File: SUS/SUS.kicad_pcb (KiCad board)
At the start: 4 copper layers, 117.7 x 30.4 mm, 72 parts, among them J1 ESP32_Connector_0, J2 ESP32_Connector_1, J3 I2C, J4 I2C, J5 I2C, J6 ADC, J7 WS, U1 TJA1051T, U2 ADS8320EB_250, U3 ICM-42688-P, U4 S1001-46R, U5 S1001-46R, U6 S1001-46R

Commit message: Complete re-design. Readme still needs to be updated.
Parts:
- removed the G*** at (106.8, 58.1)
- removed the G*** at (106.6, 59.9)
- removed the G*** at (148.9, 60.0)
- removed the G*** at (96.6, 60.1)
- removed H4: MountingHole, MountingHole:MountingHole_2.7mm_M2.5
- removed J4, J5: I2C, Connector_Hirose:Hirose_DF3EA-04P-2H_1x04-1MP_P2.00mm_Horizontal
- removed J6: ADC, Connector_Hirose:Hirose_DF3EA-03P-2H_1x03-1MP_P2.00mm_Horizontal
- removed J7: WS, Connector_Hirose:Hirose_DF3EA-03P-2H_1x03-1MP_P2.00mm_Horizontal
- removed R27: 0, Resistor_SMD:R_0402_1005Metric_Pad0.72x0.64mm_HandSolder
- removed U5, U6: S1001-46R, S1001-46R:S100146R
- added C26: 10μF, Capacitor_SMD:C_0603_1608Metric, F.Cu at (126.0, 52.5)
- added C27: 10μF, Capacitor_SMD:C_0603_1608Metric, F.Cu at (131.0, 55.2)
- added C28: 0.1μF, Capacitor_SMD:C_0201_0603Metric, F.Cu at (99.6, 54.1)
- added G***: LOGO, LOGO, F.Cu at (116.4, 55.8)
- added G***: LOGO, LOGO, F.Cu at (86.5, 56.0)
- added G***: LOGO, LOGO, F.Cu at (116.6, 54.0)
- added JP1: SolderJumper_2_Open, Jumper:SolderJumper-2_P1.3mm_Open_TrianglePad1.0x1.5mm, B.Cu at (128.1, 78.3)
- added R25: 10k, Capacitor_SMD:C_0201_0603Metric, F.Cu at (106.1, 67.7)
- C1: value 10μF -> 0.1μF; footprint Capacitor_SMD:C_0402_1005Metric_Pad0.74x0.62mm_HandSolder -> Capacitor_SMD:C_0201_0603Metric
- C2: value 1μF -> 0.1μF; footprint Capacitor_SMD:C_0402_1005Metric_Pad0.74x0.62mm_HandSolder -> Capacitor_SMD:C_0201_0603Metric
- C3: value 2.2μF -> 10nF; footprint Capacitor_SMD:C_0402_1005Metric_Pad0.74x0.62mm_HandSolder -> Capacitor_SMD:C_0201_0603Metric
- C4: value 0.1μF -> 2.2μF; footprint Capacitor_SMD:C_0402_1005Metric_Pad0.74x0.62mm_HandSolder -> Capacitor_SMD:C_0201_0603Metric
- C5: footprint Capacitor_SMD:C_0402_1005Metric_Pad0.74x0.62mm_HandSolder -> Capacitor_SMD:C_0201_0603Metric
- H1, H2, H3: value MountingHole -> MountingHole_Pad; footprint MountingHole:MountingHole_2.7mm_M2.5 -> MountingHole:MountingHole_2.2mm_M2_Pad_TopOnly
- J3: value I2C -> D25P13A4GV00LF; footprint Connector_Hirose:Hirose_DF3EA-04P-2H_1x04-1MP_P2.00mm_Horizontal -> D25:CONN_D25P_AMP
- R1, R2: footprint Resistor_SMD:R_0402_1005Metric_Pad0.72x0.64mm_HandSolder -> Capacitor_SMD:C_0201_0603Metric
- R23, R24: value 0 -> 10k; footprint Resistor_SMD:R_0402_1005Metric_Pad0.72x0.64mm_HandSolder -> Capacitor_SMD:C_0201_0603Metric
- U1: value TJA1051T -> HT7333; footprint Package_SO:SOIC-8_3.9x4.9mm_P1.27mm -> HT7333:IC_HT7333
- U2: value ADS8320EB_250 -> ADS1015IDGSR; footprint ADS8320EB_250:DGK0008A_L -> ADC:SOP50P490X110-10N
- U3: footprint IMU:ICM-42688-P -> IMU:PQFN50P300X250X97-14N
- U4: value S1001-46R -> TJA1051TK-3; footprint S1001-46R:S100146R -> Package_DFN_QFN:DFN-8-1EP_3x3mm_P0.65mm_EP1.55x2.4mm
- moved H3 101.3 mm to (132.0, 94.0)
- moved R3 65.8 mm to (134.1, 68.5), turned to 0 degrees
- moved R16 64.9 mm to (134.1, 70.5)
- moved C19 64.2 mm to (134.1, 71.4), turned to 0 degrees
- moved C6 63.7 mm to (133.0, 68.8)
- moved C18 63.6 mm to (133.0, 70.2)
- moved R17 63.5 mm to (134.1, 72.4), turned to 0 degrees
- moved R4 61.9 mm to (131.9, 68.5), turned to 0 degrees
- moved R15 61.5 mm to (131.9, 70.5), turned to 180 degrees
- moved C20 61.4 mm to (133.0, 72.1), turned to -90 degrees
- moved R1 59.9 mm to (118.2, 61.7), turned to 180 degrees
- moved C7 59.8 mm to (130.8, 68.8)
- moved R18 59.8 mm to (131.9, 72.4), turned to 0 degrees
- moved C17 59.7 mm to (130.8, 70.2)
- moved R5 58.0 mm to (129.7, 68.5), turned to 0 degrees
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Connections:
- C1 pad 1: +5V -> 5V
- C2 pad 1: +3.3V -> +5V
- J1 pad 16: CAN_S -> IMU_CS
- J1 pad 17: CAN_TX -> IMU_SCL
- J1 pad 18: CAN_RX -> IMU_MOSI
- J1 pad 19: unconnected-(J1-Pin_19-Pad19) -> IMU_MISO
- J1 pad 20: unconnected-(J1-Pin_20-Pad20) -> ESP_ADC
- J1 pad 4: I2C_SDA -> unconnected-(J1-Pin_4-Pad4)
- J1 pad 5: I2C_SCL -> unconnected-(J1-Pin_5-Pad5)
- J1 pad 7: /WS_IN -> unconnected-(J1-Pin_7-Pad7)
- J2 pad 10: IMU_MISO -> GPIO 38
- J2 pad 11: IMU_MOSI -> GPIO 37
- J2 pad 12: IMU_SCK -> GPIO 36
- J2 pad 13: IMU_CS -> GPIO 35
- J2 pad 16: unconnected-(J2-Pin_16-Pad16) -> I2C_SCL
- J2 pad 17: unconnected-(J2-Pin_17-Pad17) -> I2C_SDA
- J2 pad 19: unconnected-(J2-Pin_19-Pad19) -> GPIO 20
- J2 pad 2: unconnected-(J2-Pin_2-Pad2) -> TX
- J2 pad 20: unconnected-(J2-Pin_20-Pad20) -> GPIO 19
- J2 pad 3: unconnected-(J2-Pin_3-Pad3) -> RX
- J2 pad 4: Net-(J2-Pin_4) -> CAN_TX
- J2 pad 5: A_SCK -> CAN_RX
- J2 pad 6: A_MISO -> CAN_S
- J2 pad 7: A_CS -> A_SCL
- J2 pad 8: unconnected-(J2-Pin_8-Pad8) -> A_SDA
- J2 pad 9: unconnected-(J2-Pin_9-Pad9) -> A_CS
- J3 pad 1: +5V -> +12V
- J3 pad 2: GND -> GPIO 19
- J3 pad 3: CAN- -> GPIO 20
- J3 pad 4: CAN+ -> GND
- R23 pad 2: Net-(J6-Pin_1) -> A_SCL
- R24 pad 1: +5V -> +3.3V
- R24 pad 2: Net-(J6-Pin_1) -> A_SDA
- U1 pad 1: CAN_TX -> GND
- U1 pad 2: GND -> +12V
- U2 pad 1: +5V -> GND
- U2 pad 2: AA_out -> A_CS
- U2 pad 4: GND -> AA_out
- U2 pad 5: A_CS -> GND
- U2 pad 6: A_MISO -> unconnected-(U2-AIN2-Pad6)
- U2 pad 7: A_SCK -> unconnected-(U2-AIN3-Pad7)
- U2 pad 8: +3.3V -> 5V
- U3 pad 13: IMU_SCK -> IMU_SCL
- U4 pad 1: GND -> CAN_TX
- U4 pad 3: GND -> +5V
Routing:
- net GND: track 99.6 -> 47.6 mm, vias 71 -> 14
- net /WS_IN: track 44.5 -> 0.00 mm
- net CAN+: track 53.4 -> 10.9 mm
- net CAN-: track 52.6 -> 11.0 mm
- net GPIO 20: track 0.00 -> 20.6 mm
- net GPIO 19: track 0.00 -> 20.5 mm
- net RX: track 0.00 -> 20.5 mm
- net TX: track 0.00 -> 20.4 mm
- net GPIO 36: track 0.00 -> 19.1 mm
- net GPIO 37: track 0.00 -> 18.5 mm
- net A_In: track 18.1 -> 36.5 mm
- net A_SCL: track 0.00 -> 18.2 mm
- net GPIO 35: track 0.00 -> 18.0 mm
- net GPIO 38: track 0.00 -> 17.7 mm
- net A_SDA: track 0.00 -> 14.1 mm
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- added copper zone on B.Cu, net +3.3V
- added copper zone on In1.Cu, net +5V
- removed copper zone on In1.Cu, net +3.3V
- removed copper zone on B.Cu, net +5V
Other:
- board size 117.7 x 30.4 mm -> 58 x 64 mm
- board text added: "12V"
- board text added: "19"
- board text added: "20"
- board text added: "35"
- board text added: "36"
- board text added: "37"
- board text added: "38"
- board text added: "A_IN"
- board text added: "CH"
- board text added: "CL"
- board text added: "NC"
- board text added: "RX"
- board text added: "SCL"
- board text added: "SDA"
- board text added: "TX"
- board text removed: "CAN"
- board text removed: "DLHR"
- board text removed: "ESP_ADC"
- board text removed: "LP"
- board text removed: "U3"
- board text removed: "WS"

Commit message: Updated Readme
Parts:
- moved H1 0.89 mm to (107.0, 55.0)
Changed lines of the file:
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@@
 	(footprint "MountingHole:MountingHole_2.2mm_M2_Pad_TopOnly"
 		(layer "F.Cu")
-		(at 107.4 55.8)
+		(at 107 55)
 		(descr "Mounting Hole 2.2mm, M2")
 		(tags "mounting hole 2.2mm m2")
@@
 		(layer "Edge.Cuts")
 	)
+	(gr_line
+		(start 107 94)
+		(end 107 96)
+		(stroke
+			(width 0.1)
+			(type default)
+		)
+		(layer "User.1")
+	)
+	(gr_line
+		(start 107 55)
+		(end 107 94)
+		(stroke
+			(width 0.1)
+			(type default)
+		)
+		(layer "User.1")
+	)
 	(gr_text "CH"
 		(at 96.2 48.9 0)
@@
 		)
 	)
+	(dimension
+		(type aligned)
+		(layer "User.1")
+		(pts
+			(xy 132 94) (xy 82 94)
+		)
+		(height -7)
+		(gr_text "50.0000 mm"
+			(at 107 99.85 0)
+			(layer "User.1")
+			(effects
+				(font
+					(size 1 1)
+					(thickness 0.15)
+				)
+			)
+		)
+		(format
+			(prefix "")
+			(suffix "")
+			(units 3)
+			(units_format 1)
+			(precision 4)
+		)
+		(style
+			(thickness 0.1)
+			(arrow_length 1.27)
+			(text_position_mode 0)
+			(extension_height 0.58642)
+			(extension_offset 0.5) keep_text_aligned)
+	)
+	(dimension
+		(type aligned)
+		(layer "User.1")
+		(pts
+			(xy 107 55) (xy 107 94)
+		)
+		(height 38)
+		(gr_text "39.0000 mm"
+			(at 67.85 74.5 90)
+			(layer "User.1")
+			(effects
+				(font
+					(size 1 1)
+					(thickness 0.15)
+				)
+			)
+		)
+		(format
+			(prefix "")
+			(suffix "")
+			(units 3)
+			(units_format 1)
+			(precision 4)
+		)
+		(style
+			(thickness 0.1)
+			(arrow_length 1.27)
+			(text_position_mode 0)
+			(extension_height 0.58642)
+			(extension_offset 0.5) keep_text_aligned)
+	)
+	(dimension
+		(type aligned)
+		(layer "User.1")
+		(pts
+			(xy 107 94) (xy 82 94)
+		)
+		(height -4)
+		(gr_text "25.0000 mm"
+			(at 94.5 96.85 0)
+			(layer "User.1")
+			(effects
+				(font
+					(size 1 1)
+					(thickness 0.15)
+				)
+			)
+		)
+		(format
+			(prefix "")
+			(suffix "")
+			(units 3)
+			(units_format 1)
+			(precision 4)
+		)
+		(style
+			(thickness 0.1)
+			(arrow_length 1.27)
+			(text_position_mode 0)
+			(extension_height 0.58642)
+			(extension_offset 0.5) keep_text_aligned)
+	)
 	(segment
 		(start 110 81.226898)
@@
 	)
 	(segment
-		(start 104.35 48.974144)
-		(end 104.35 63.25)
+		(start 104 62.9)
+		(end 105.2 64.1)
 		(width 0.3)
 		(layer "F.Cu")
@@
 	)
 	(segment
-		(start 104.35 63.25)
-		(end 105.2 64.1)
+		(start 106.479994 46.84415)
+		(end 104 49.324144)
 		(width 0.3)
 		(layer "F.Cu")
@@
 	)
 	(segment
-		(start 106.479994 46.84415)
-		(end 104.35 48.974144)
+		(start 104 49.324144)
+		(end 104 62.9)
 		(width 0.3)
 		(layer "F.Cu")

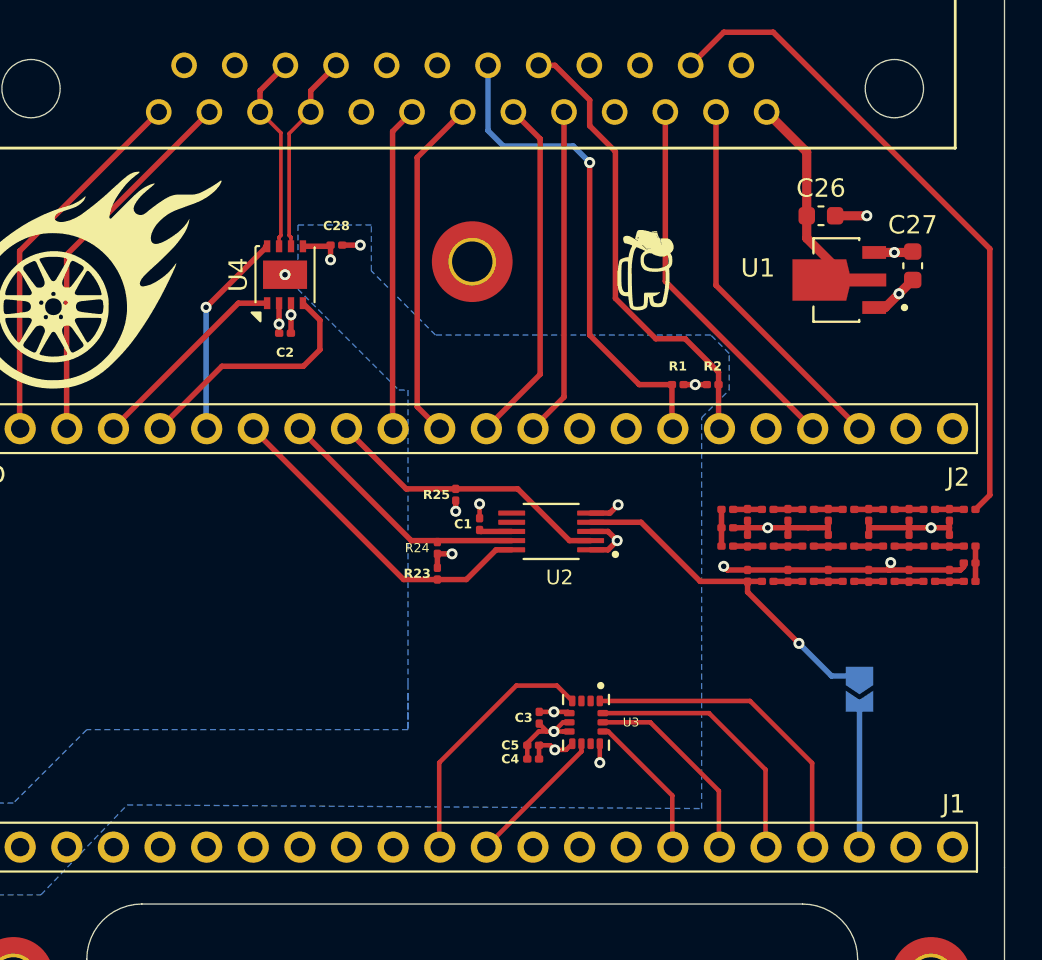
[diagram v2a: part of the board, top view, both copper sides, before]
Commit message: Changed CAN transceiver.
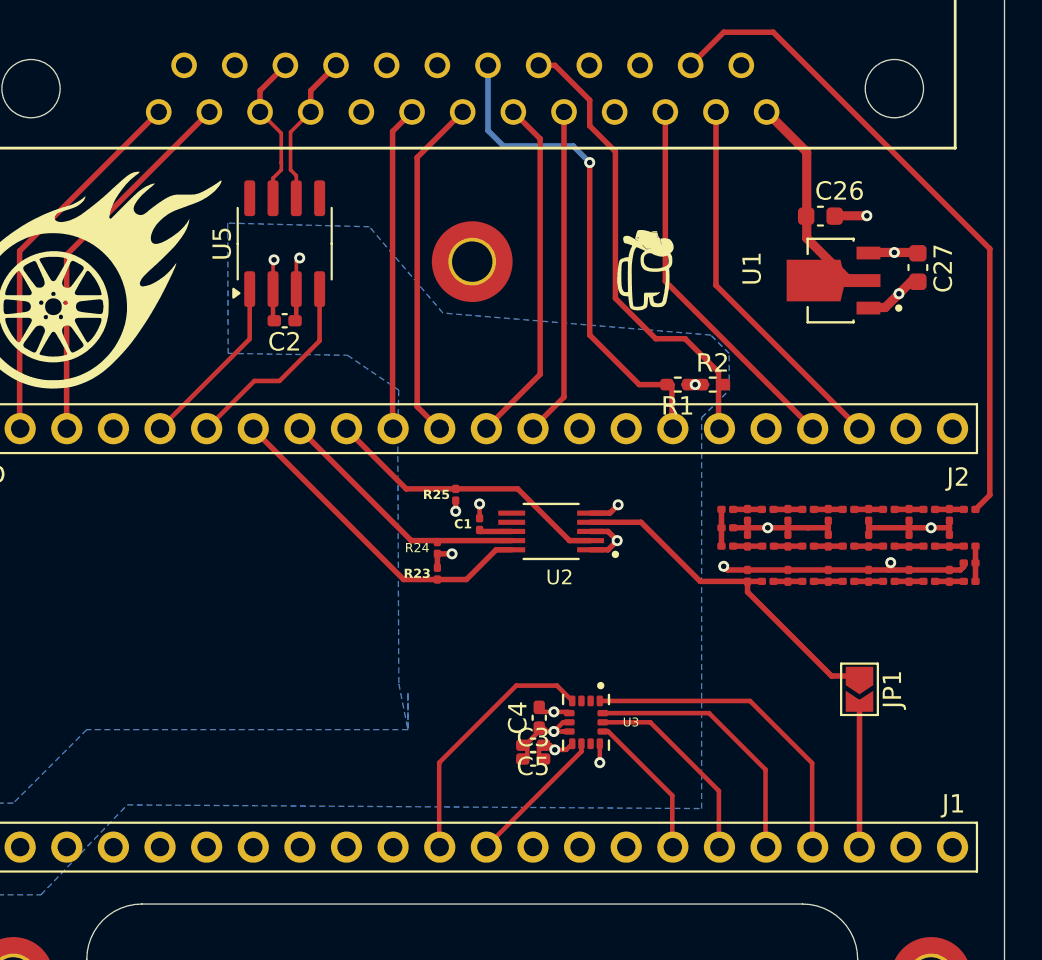
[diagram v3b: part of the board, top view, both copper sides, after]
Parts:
- removed C28: 0.1μF, Capacitor_SMD:C_0201_0603Metric
- removed U4: TJA1051TK-3, Package_DFN_QFN:DFN-8-1EP_3x3mm_P0.65mm_EP1.55x2.4mm
- added U5: SN65HVD232, Package_SO:SOIC-8_3.9x4.9mm_P1.27mm, F.Cu at (96.8, 54.0)
- C2, C5: footprint Capacitor_SMD:C_0201_0603Metric -> Capacitor_SMD:C_0402_1005Metric_Pad0.74x0.62mm_HandSolder
- C26: value 10μF -> 0.33μF
- C27: value 10μF -> 0.1μF
- C3: renamed from C4; footprint Capacitor_SMD:C_0201_0603Metric -> Capacitor_SMD:C_0402_1005Metric_Pad0.74x0.62mm_HandSolder
- C4: renamed from C3; value 10nF -> 0.1μF; footprint Capacitor_SMD:C_0201_0603Metric -> Capacitor_SMD:C_0402_1005Metric_Pad0.74x0.62mm_HandSolder
- JP1: moved to F.Cu
- R1, R2: footprint Capacitor_SMD:C_0201_0603Metric -> Resistor_SMD:R_0402_1005Metric_Pad0.72x0.64mm_HandSolder
- moved C2 0.68 mm to (96.8, 58.2)
- moved U1 0.31 mm to (126.7, 56.0)
- moved C27 0.30 mm to (131.3, 55.3)
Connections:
- C2 pad 1: +5V -> +3.3V
- J1 pad 17: IMU_SCL -> IMU_MOSI
- J1 pad 18: IMU_MOSI -> IMU_SCL
- J2 pad 4: CAN_TX -> unconnected-(J2-Pin_4-Pad4)
- J2 pad 5: CAN_RX -> CAN_TX
- J2 pad 6: CAN_S -> CAN_RX
- J3 pad 2: GPIO 19 -> GPIO 20
- J3 pad 25: GND -> unconnected-(J3-Pad25)
- J3 pad 3: GPIO 20 -> GPIO 19
- U2 pad 5: GND -> unconnected-(U2-AIN1-Pad5)
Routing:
- net CAN_S: track 11.4 -> 0.00 mm, vias 1 -> 0
- net CAN-: track 11.0 -> 8.40 mm
- net CAN_RX: track 13.4 -> 11.0 mm
- net CAN+: track 10.9 -> 8.48 mm
- net unconnected-(U2-AIN1-Pad5): track 0.00 -> 1.69 mm, vias 0 -> 1
- net +5V: track 3.76 -> 2.12 mm, vias 2 -> 1
- net CAN_TX: track 11.2 -> 9.63 mm
- net +3.3V: track 10.6 -> 11.9 mm
- net GND: track 47.6 -> 46.7 mm, vias 14 -> 11
- net AA_out: vias 1 -> 0

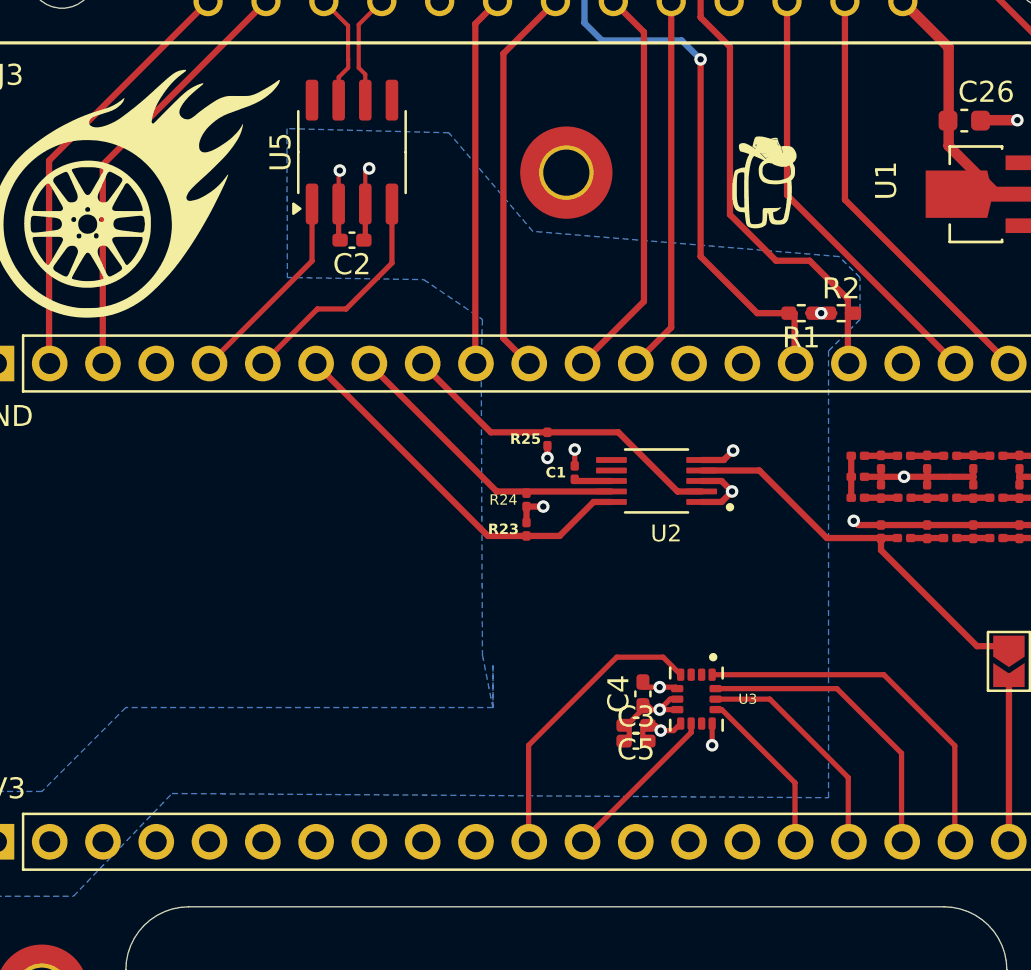
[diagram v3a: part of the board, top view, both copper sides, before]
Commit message: Fixed DRC errors
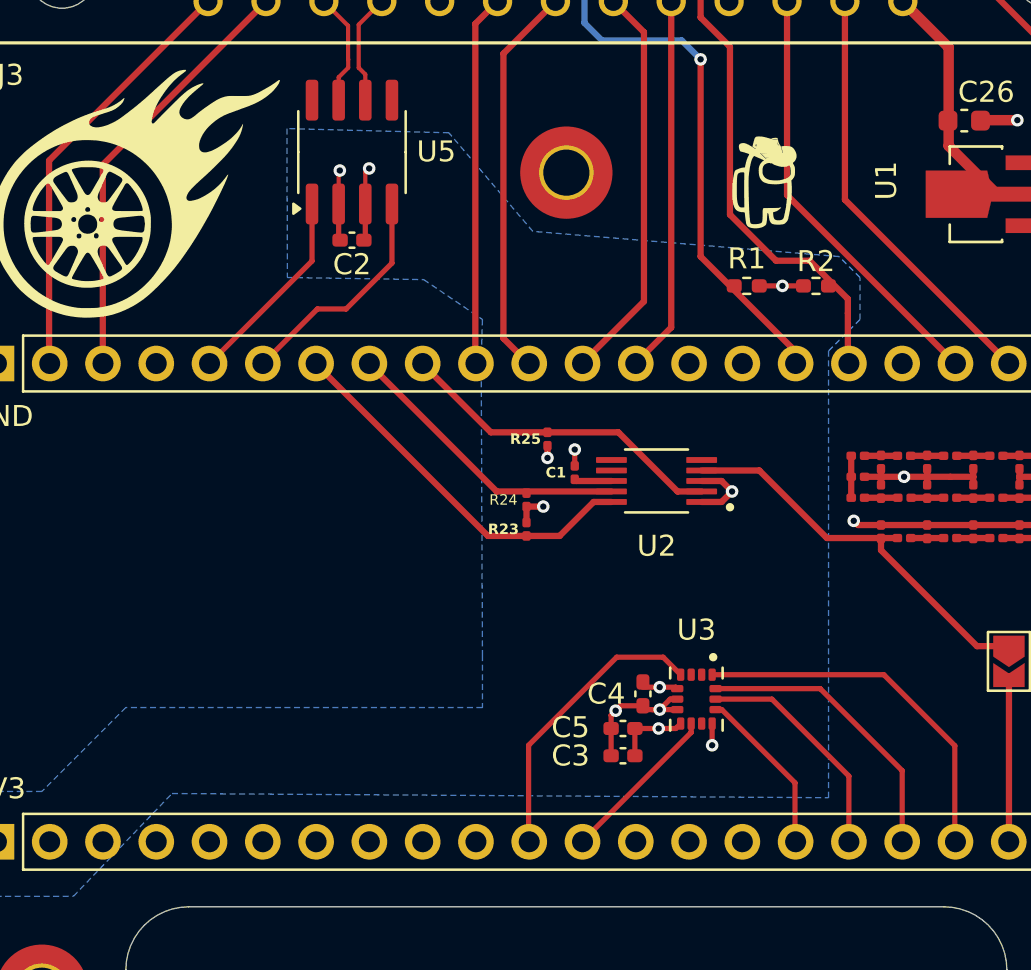
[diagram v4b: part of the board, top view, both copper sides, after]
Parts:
- moved R1 2.91 mm to (115.6, 60.4)
- moved R2 1.77 mm to (118.9, 60.4)
- moved C3 0.94 mm to (109.7, 82.8)
- moved C5 0.64 mm to (109.7, 81.5)
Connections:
- J1 pad 17: IMU_MOSI -> IMU_SCL
- J1 pad 18: IMU_SCL -> IMU_MOSI
- J3 pad 2: GPIO 20 -> GPIO 19
- J3 pad 3: GPIO 19 -> GPIO 20
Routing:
- net unconnected-(U2-AIN1-Pad5): track 1.69 -> 0.00 mm, vias 1 -> 0
- net +3.3V: track 11.9 -> 13.4 mm
- net GND: track 46.7 -> 48.0 mm, vias 11 -> 12
- net I2C_SCL: track 27.2 -> 26.2 mm
